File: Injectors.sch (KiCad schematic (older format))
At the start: 36 parts, among them Q1 VND14NV04, Q2 VND14NV04, Q3 VND14NV04, Q4 VND14NV04, Q5 VND14NV04, Q6 VND14NV04

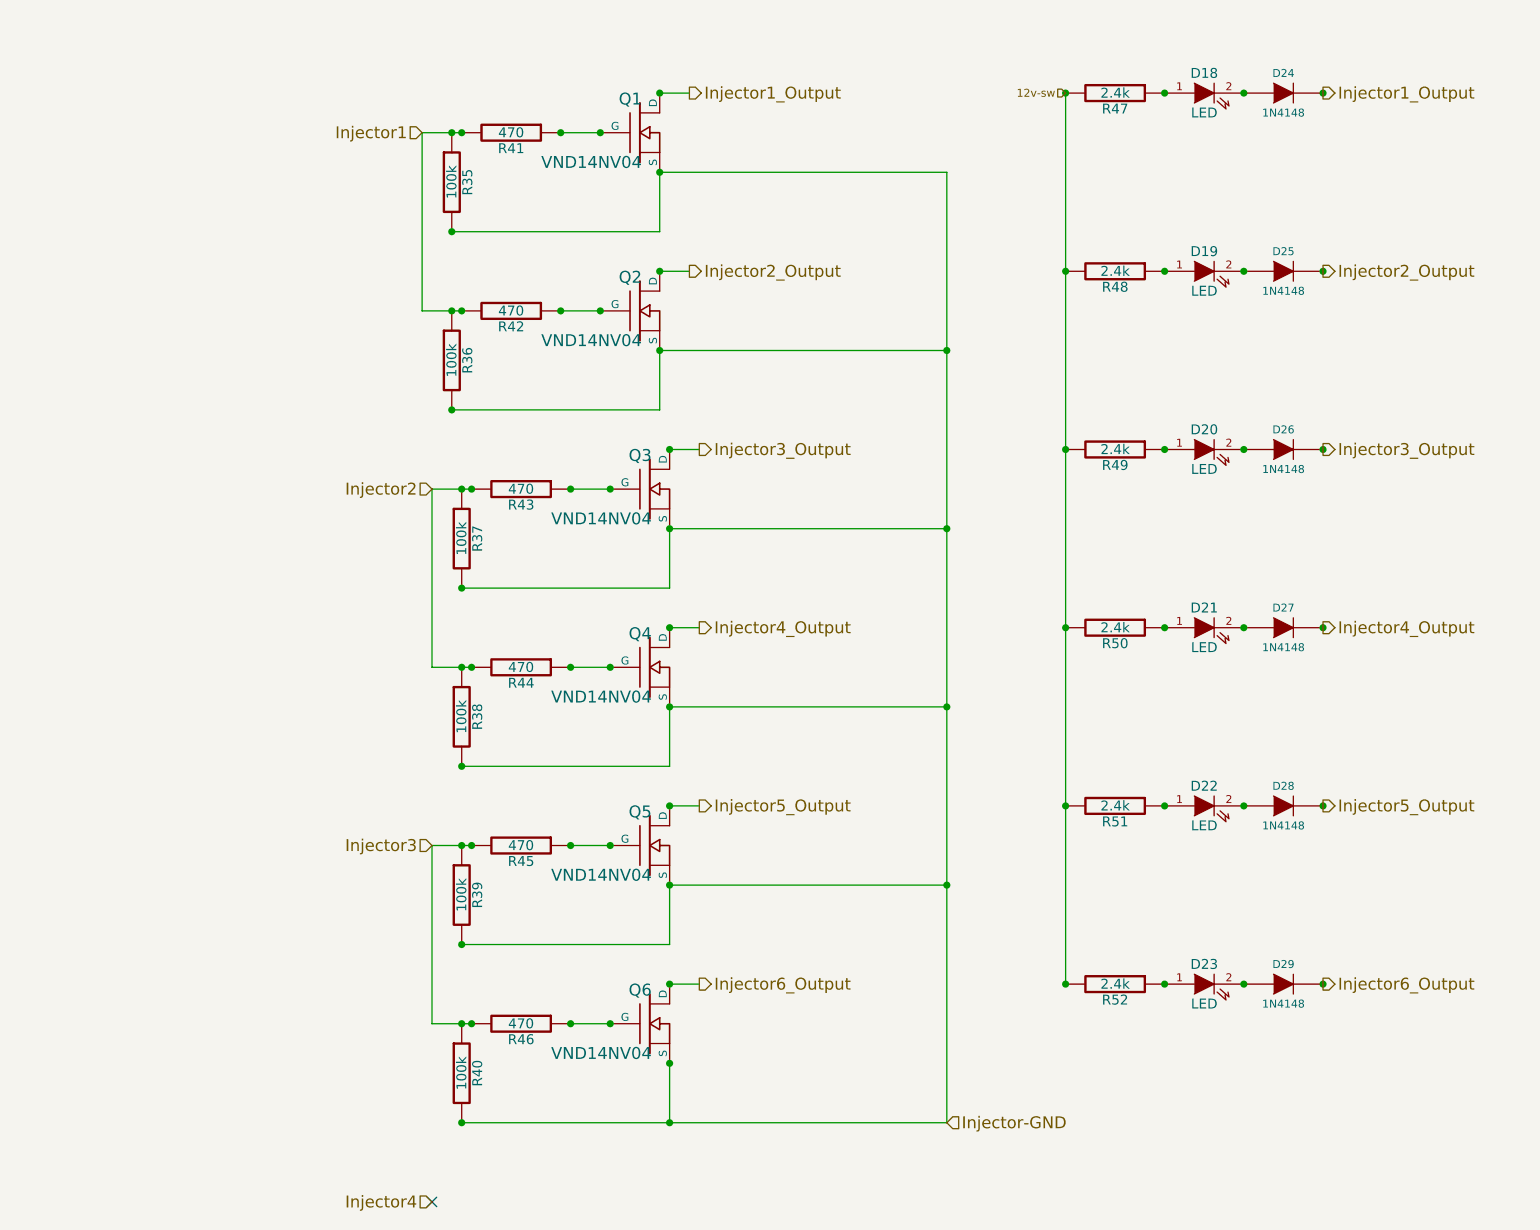
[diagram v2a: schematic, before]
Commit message: Modified: schematics to correct errors
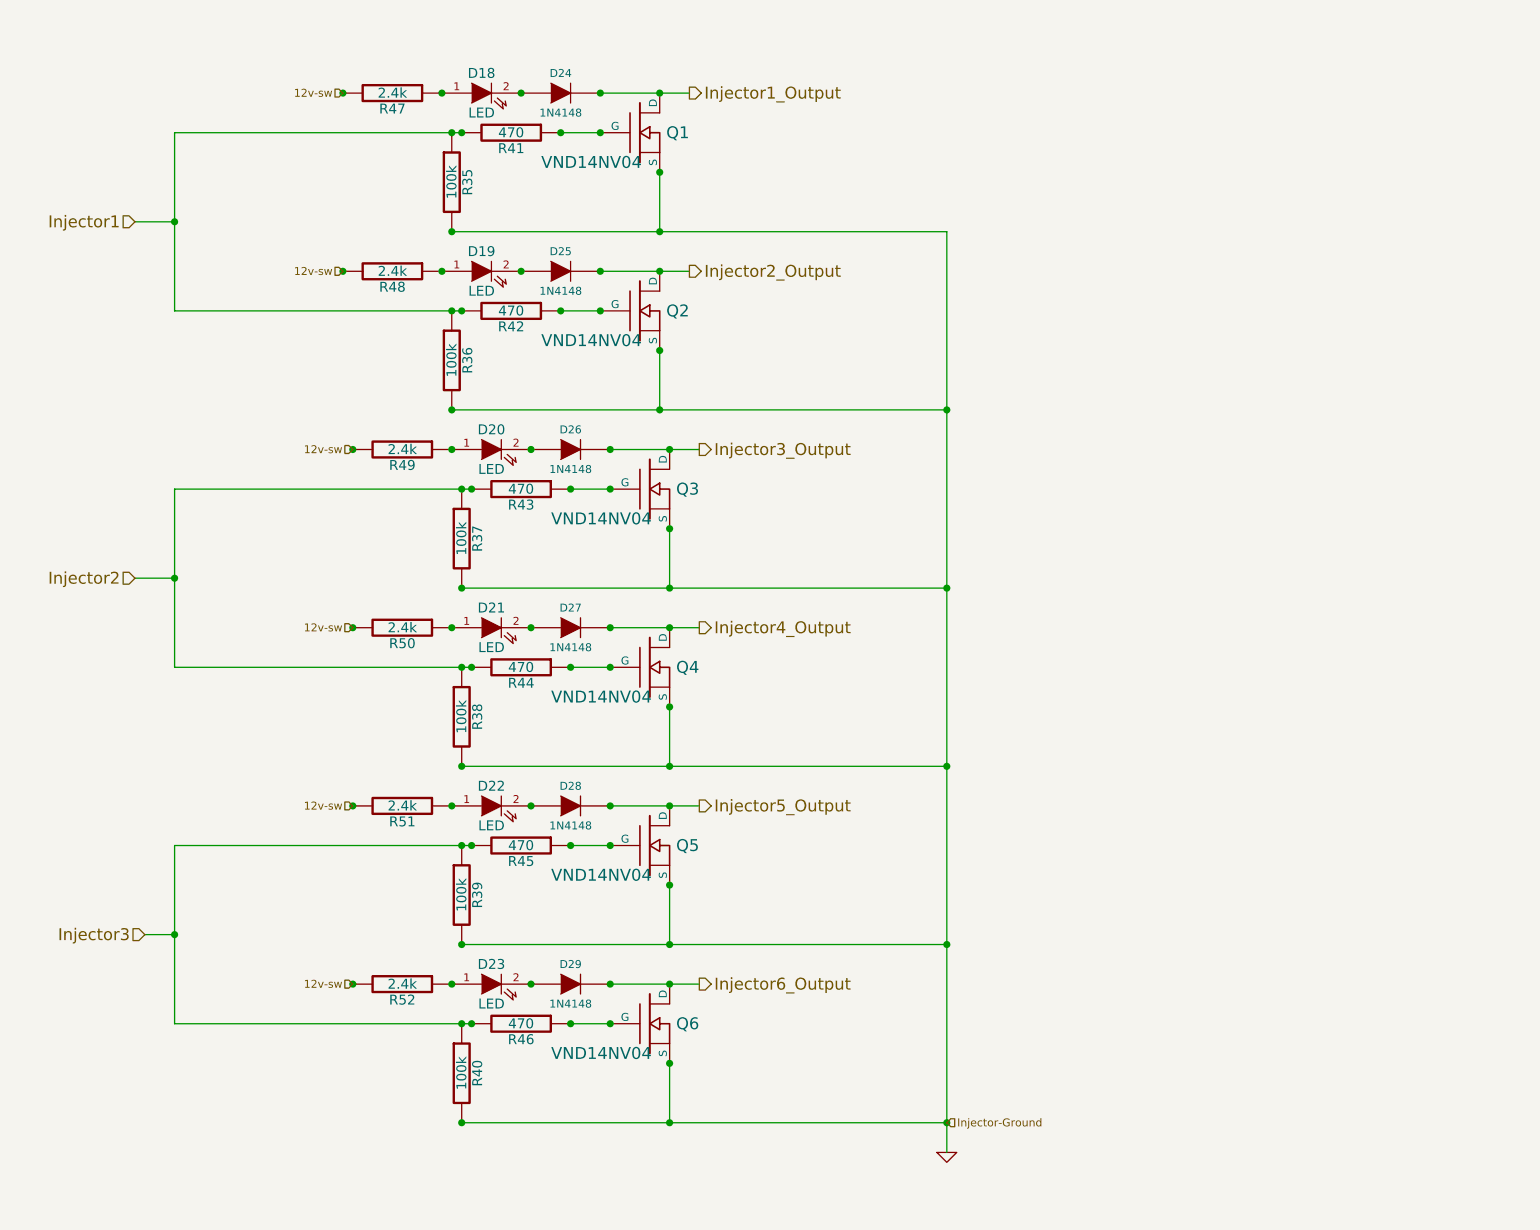
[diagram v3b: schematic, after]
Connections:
- net Injector-GND renamed GND
- no-connect marks 1 -> 0
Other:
- moved on the sheet: D18, D19, D20, D21, D22, D23, D24, D25, D26, D27, D28, D29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

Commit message: Improved schematic, re-design board, re-created PDF
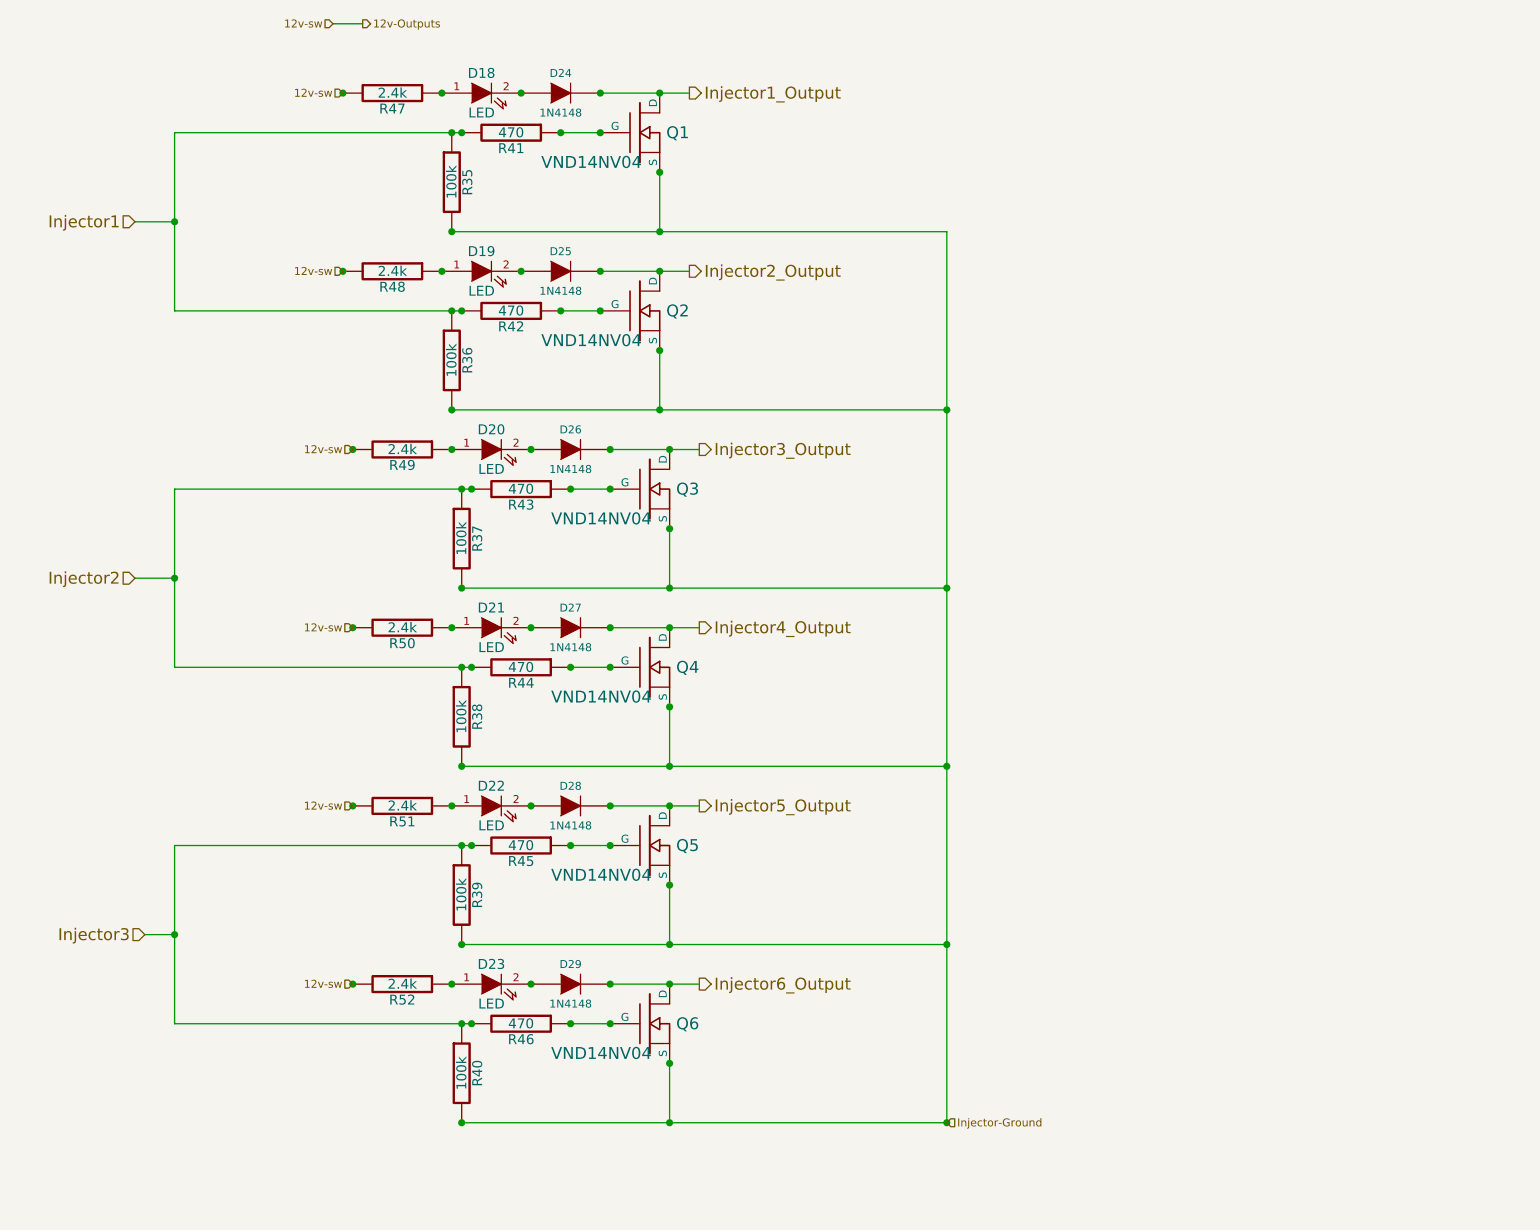
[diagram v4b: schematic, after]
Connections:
- net 12v-sw renamed 12v-Outputs
- net GND renamed Injector-Ground
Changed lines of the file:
@@
-EESchema Schematic File Version 2  date Sun 22 Jan 2012 05:59:51 PM EST
+EESchema Schematic File Version 2  date Mon 23 Jan 2012 07:28:42 AM EST
 LIBS:power
 LIBS:device
@@
 EELAYER END
 $Descr A4 11700 8267
-Sheet 3 7
-Title "Injector Drivers"
-Date "22 jan 2012"
-Rev "A"
-Comp "Jaguar board for FreeEMS"
+Sheet 4 7
+Title "Jaguar PCB for FreeEMS"
+Date "23 jan 2012"
+Rev "A.1"
+Comp "diyefi.org"
 Comment1 ""
 Comment2 ""
@@
 $EndDescr
 Wire Wire Line
+	2300 900  2450 900
+Wire Wire Line
+	2950 2350 1500 2350
+Wire Wire Line
+	1500 2350 1500 1450
+Wire Wire Line
+	1500 1450 2950 1450
+Connection ~ 3700 5750
+Connection ~ 3700 4850
+Wire Wire Line
+	3700 4850 4150 4850
+Wire Wire Line
+	3700 3050 4150 3050
+Wire Wire Line
+	3000 3250 1500 3250
+Wire Wire Line
+	1500 3250 1500 4150
+Wire Wire Line
+	1500 4150 3000 4150
+Connection ~ 3950 1950
+Wire Wire Line
+	2900 1950 5400 1950
+Connection ~ 4000 3750
+Connection ~ 5400 3750
+Wire Wire Line
+	5400 3750 2950 3750
+Connection ~ 4000 5550
+Connection ~ 5400 5550
+Wire Wire Line
+	5400 5550 2950 5550
+Wire Wire Line
+	3000 5050 1500 5050
+Wire Wire Line
+	1500 5050 1500 5950
+Connection ~ 4000 6450
+Connection ~ 3950 1250
+Wire Wire Line
+	4000 6450 4000 6150
+Connection ~ 2950 6450
+Wire Wire Line
+	3700 5950 3500 5950
+Connection ~ 4000 5750
+Connection ~ 4000 6150
+Connection ~ 3700 5950
+Connection ~ 3500 5950
+Connection ~ 3000 5950
+Connection ~ 2950 5950
+Connection ~ 2950 5050
+Connection ~ 3000 5050
+Connection ~ 3500 5050
+Connection ~ 3700 5050
+Connection ~ 4000 5250
+Connection ~ 4000 4850
+Wire Wire Line
+	3700 5050 3500 5050
+Connection ~ 2950 5550
+Wire Wire Line
+	4000 5250 4000 5550
+Wire Wire Line
+	4000 4650 4000 4350
+Connection ~ 2950 4650
+Wire Wire Line
+	3700 4150 3500 4150
+Connection ~ 4000 3950
+Connection ~ 4000 4350
+Connection ~ 3700 4150
+Connection ~ 3500 4150
+Connection ~ 3000 4150
+Connection ~ 2950 4150
+Wire Wire Line
+	4000 3450 4000 3750
+Connection ~ 2950 3750
+Wire Wire Line
+	3700 3250 3500 3250
+Connection ~ 4000 3050
+Connection ~ 4000 3450
+Connection ~ 3700 3250
+Connection ~ 3500 3250
+Connection ~ 3000 3250
+Connection ~ 2950 3250
+Wire Wire Line
+	3950 2850 3950 2550
+Connection ~ 2900 2850
+Wire Wire Line
+	3650 2350 3450 2350
+Connection ~ 3950 2150
+Connection ~ 3950 2550
+Connection ~ 3650 2350
+Connection ~ 3450 2350
+Connection ~ 2950 2350
+Connection ~ 2900 2350
+Connection ~ 2900 1450
+Connection ~ 2950 1450
+Connection ~ 3450 1450
+Connection ~ 3650 1450
+Connection ~ 3950 1650
+Wire Wire Line
+	3650 1450 3450 1450
+Connection ~ 2900 1950
+Wire Wire Line
+	3950 1950 3950 1650
+Connection ~ 3250 1250
+Connection ~ 2850 1250
+Connection ~ 2850 2150
+Connection ~ 3250 2150
+Connection ~ 3300 3050
+Connection ~ 2900 3050
+Connection ~ 2900 3950
+Connection ~ 3300 3950
+Connection ~ 3300 4850
+Connection ~ 2900 4850
+Connection ~ 2900 5750
+Connection ~ 3300 5750
+Connection ~ 3650 1250
+Connection ~ 3650 2150
+Connection ~ 5400 6450
+Connection ~ 2400 5750
+Wire Wire Line
+	1500 5950 3000 5950
+Wire Wire Line
+	1350 5500 1500 5500
+Connection ~ 1500 5500
+Wire Wire Line
+	2950 6450 5400 6450
+Wire Wire Line
+	5400 4650 2950 4650
+Connection ~ 5400 4650
+Connection ~ 4000 4650
+Wire Wire Line
+	5400 2850 2900 2850
+Connection ~ 5400 2850
+Connection ~ 3950 2850
+Connection ~ 2400 4850
+Connection ~ 2400 3950
+Wire Wire Line
+	1300 3700 1500 3700
+Connection ~ 1500 3700
+Wire Wire Line
+	3700 3950 4150 3950
+Connection ~ 3700 3950
+Connection ~ 3700 3050
+Wire Wire Line
+	3650 1250 4100 1250
+Connection ~ 2350 1250
+Connection ~ 2350 2150
+Connection ~ 2400 3050
+Wire Wire Line
+	3700 5750 4150 5750
+Wire Wire Line
+	1300 1900 1500 1900
+Connection ~ 1500 1900
+Wire Wire Line
 	3650 2150 4100 2150
-Connection ~ 1500 1900
-Wire Wire Line
-	1300 1900 1500 1900
-Wire Wire Line
-	3700 5750 4150 5750
-Connection ~ 2400 3050
-Connection ~ 2350 2150
-Connection ~ 2350 1250
-Wire Wire Line
-	3650 1250 4100 1250
-Connection ~ 3700 3050
-Connection ~ 3700 3950
-Wire Wire Line
-	3700 3950 4150 3950
-Connection ~ 1500 3700
-Wire Wire Line
-	1300 3700 1500 3700
-Connection ~ 2400 3950
-Connection ~ 2400 4850
-Connection ~ 3950 2850
-Connection ~ 5400 2850
-Wire Wire Line
-	5400 2850 2900 2850
-Connection ~ 4000 4650
-Connection ~ 5400 4650
-Wire Wire Line
-	5400 4650 2950 4650
-Wire Wire Line
-	2950 6450 5400 6450
-Connection ~ 1500 5500
-Wire Wire Line
-	1350 5500 1500 5500
-Wire Wire Line
-	3000 5950 1500 5950
-Connection ~ 2400 5750
-Connection ~ 5400 6450
-Connection ~ 3650 2150
-Connection ~ 3650 1250
-Connection ~ 3300 5750
-Connection ~ 2900 5750
-Connection ~ 2900 4850
-Connection ~ 3300 4850
-Connection ~ 3300 3950
-Connection ~ 2900 3950
-Connection ~ 2900 3050
-Connection ~ 3300 3050
-Connection ~ 3250 2150
-Connection ~ 2850 2150
-Connection ~ 2850 1250
-Connection ~ 3250 1250
-Wire Wire Line
-	3950 1950 3950 1650
-Connection ~ 2900 1950
-Wire Wire Line
-	3650 1450 3450 1450
-Connection ~ 3950 1650
-Connection ~ 3650 1450
-Connection ~ 3450 1450
-Connection ~ 2950 1450
-Connection ~ 2900 1450
-Connection ~ 2900 2350
-Connection ~ 2950 2350
-Connection ~ 3450 2350
-Connection ~ 3650 2350
-Connection ~ 3950 2550
-Connection ~ 3950 2150
-Wire Wire Line
-	3650 2350 3450 2350
-Connection ~ 2900 2850
-Wire Wire Line
-	3950 2850 3950 2550
-Connection ~ 2950 3250
-Connection ~ 3000 3250
-Connection ~ 3500 3250
-Connection ~ 3700 3250
-Connection ~ 4000 3450
-Connection ~ 4000 3050
-Wire Wire Line
-	3700 3250 3500 3250
-Connection ~ 2950 3750
-Wire Wire Line
-	4000 3450 4000 3750
-Connection ~ 2950 4150
-Connection ~ 3000 4150
-Connection ~ 3500 4150
-Connection ~ 3700 4150
-Connection ~ 4000 4350
-Connection ~ 4000 3950
-Wire Wire Line
-	3700 4150 3500 4150
-Connection ~ 2950 4650
-Wire Wire Line
-	4000 4650 4000 4350
-Wire Wire Line
-	4000 5250 4000 5550
-Connection ~ 2950 5550
-Wire Wire Line
-	3700 5050 3500 5050
-Connection ~ 4000 4850
-Connection ~ 4000 5250
-Connection ~ 3700 5050
-Connection ~ 3500 5050
-Connection ~ 3000 5050
-Connection ~ 2950 5050
-Connection ~ 2950 5950
-Connection ~ 3000 5950
-Connection ~ 3500 5950
-Connection ~ 3700 5950
-Connection ~ 4000 6150
-Connection ~ 4000 5750
-Wire Wire Line
-	3700 5950 3500 5950
-Connection ~ 2950 6450
-Wire Wire Line
-	4000 6450 4000 6150
-Connection ~ 3950 1250
-Connection ~ 4000 6450
-Wire Wire Line
-	1500 5950 1500 5050
-Wire Wire Line
-	1500 5050 3000 5050
-Wire Wire Line
-	5400 5550 2950 5550
-Connection ~ 5400 5550
-Connection ~ 4000 5550
-Wire Wire Line
-	5400 3750 2950 3750
-Connection ~ 5400 3750
-Connection ~ 4000 3750
-Wire Wire Line
-	2900 1950 5400 1950
-Connection ~ 3950 1950
-Wire Wire Line
-	3000 4150 1500 4150
-Wire Wire Line
-	1500 4150 1500 3250
-Wire Wire Line
-	1500 3250 3000 3250
-Wire Wire Line
-	3700 3050 4150 3050
-Wire Wire Line
-	3700 4850 4150 4850
-Connection ~ 3700 4850
-Connection ~ 3700 5750
-Wire Wire Line
-	2950 1450 1500 1450
-Wire Wire Line
-	1500 1450 1500 2350
-Wire Wire Line
-	1500 2350 2950 2350
-Wire Wire Line
-	5400 1950 5400 6600
+Wire Wire Line
+	5400 6450 5400 1950
+Text HLabel 2450 900  2    40   Output ~ 0
+12v-Outputs
+Text HLabel 2300 900  0    40   Input ~ 0
+12v-sw
 Text HLabel 2400 5750 0    40   Input ~ 0
 12v-sw
@@
 Text HLabel 2350 2150 0    40   Input ~ 0
 12v-sw
-$Comp
-L GND #PWR55
-U 1 1 4F1C44F4
-P 5400 6600
-F 0 "#PWR55" H 5400 6600 30  0001 C CNN
-F 1 "GND" H 5400 6530 30  0001 C CNN
-	1    5400 6600
-	1    0    0    -1
-$EndComp
 Text HLabel 5400 6450 2    40   Input ~ 0
 Injector-Ground
